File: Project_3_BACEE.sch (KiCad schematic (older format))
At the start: 13 parts, among them U1 24LC1025, U2 24LC1025, U3 DS1337S+, U4 ATMEGA328P-AU, Y1 Crystal 32 MHz, Y2 Crystal 16 MHz

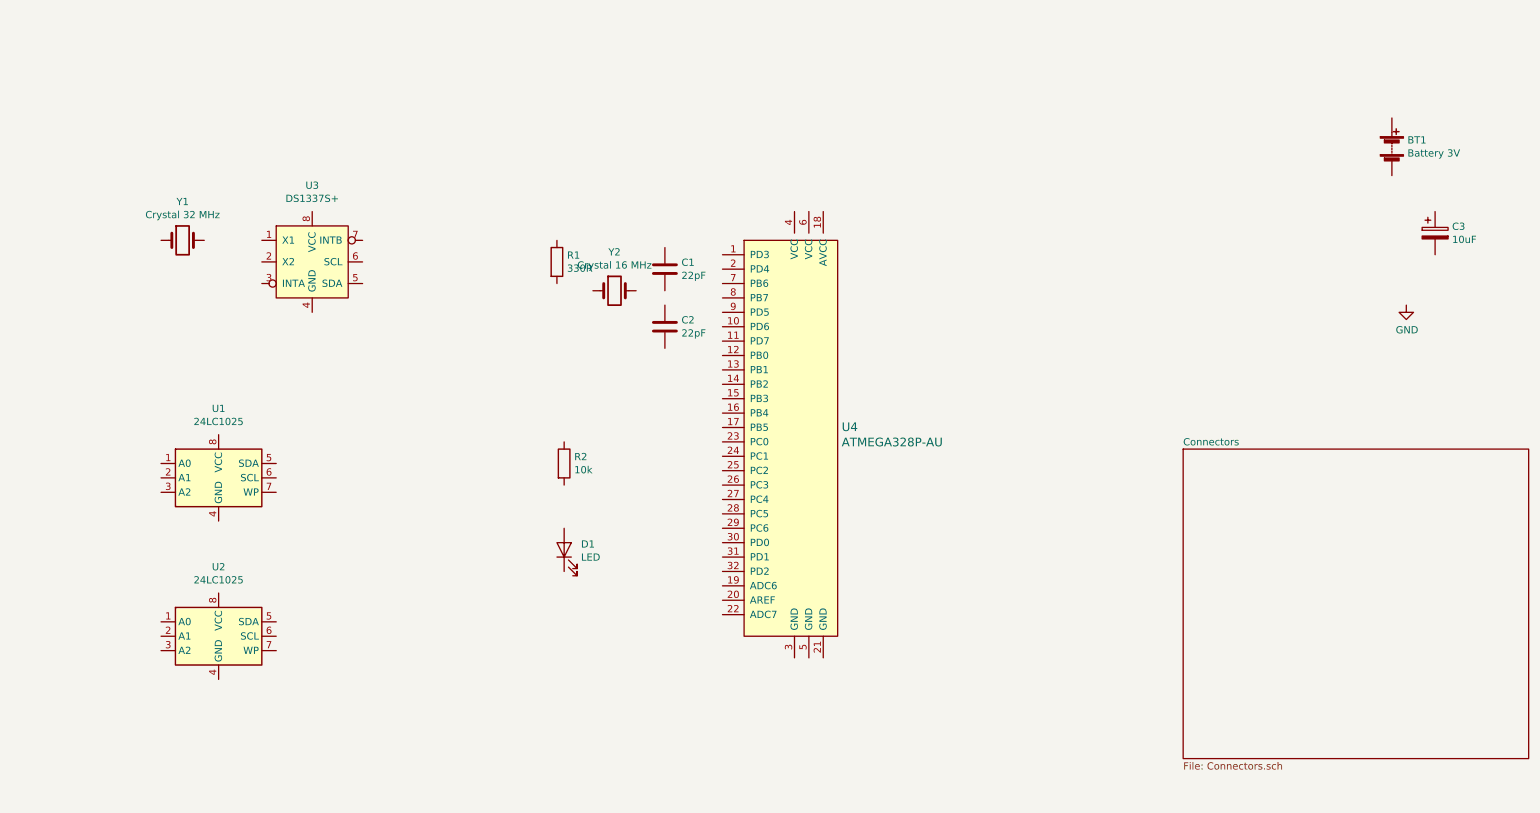
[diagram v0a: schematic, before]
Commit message: Completed wiring and connectors sheet.
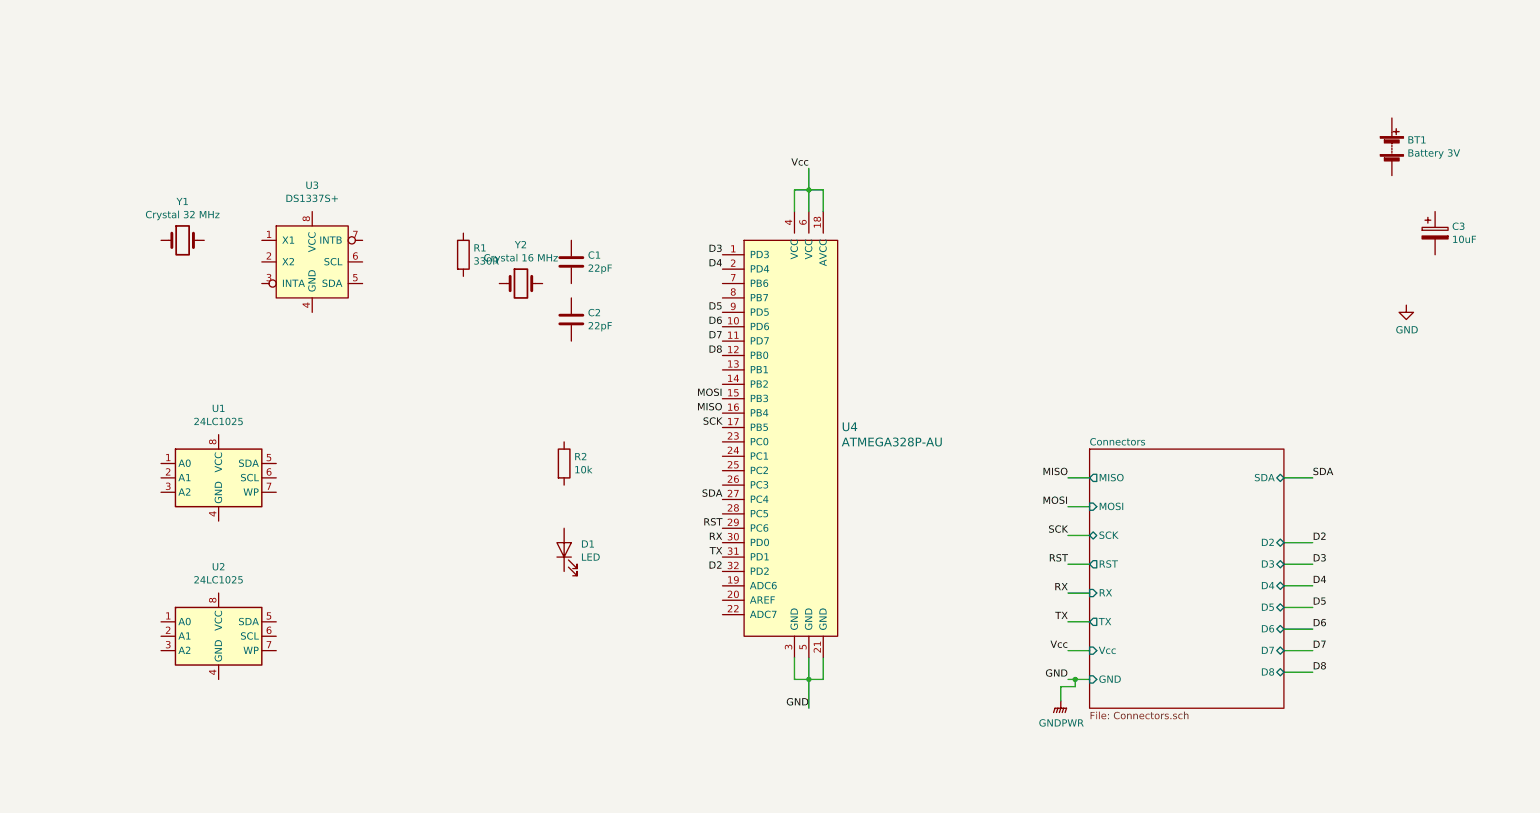
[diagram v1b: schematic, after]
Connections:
- net GND: now also U4.21 (GND), U4.3 (GND), U4.5 (GND)
- net D3: now reaches U4.1 (PD3)
- net D6: now reaches U4.10 (PD6)
- net D7: now reaches U4.11 (PD7)
- net D8: now reaches U4.12 (PB0)
- net MOSI: now reaches U4.15 (PB3)
- net MISO: now reaches U4.16 (PB4)
- net SCK: now reaches U4.17 (PB5)
- net Vcc: now reaches U4.18 (AVCC)
- net Vcc: now also U4.4 (VCC), U4.6 (VCC)
- net D4: now reaches U4.2 (PD4)
- net SDA: now reaches U4.27 (PC4)
- net RST: now reaches U4.29 (PC6)
- net RX: now reaches U4.30 (PD0)
- net TX: now reaches U4.31 (PD1)
- net D2: now reaches U4.32 (PD2)
- net D5: now reaches U4.9 (PD5)
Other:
- moved on the sheet: C1, C2, R1, Y2
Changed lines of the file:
@@
 L Device:C C1
 U 1 1 5D837139
-P 5100 2650
-F 0 "C1" H 5215 2696 50  0000 L CNN
-F 1 "22pF" H 5215 2605 50  0000 L CNN
-F 2 "Capacitor_SMD:C_0805_2012Metric_Pad1.15x1.40mm_HandSolder" H 5138 2500 50  0001 C CNN
-F 3 "~" H 5100 2650 50  0001 C CNN
-	1    5100 2650
+P 4450 2600
+F 0 "C1" H 4565 2646 50  0000 L CNN
+F 1 "22pF" H 4565 2555 50  0000 L CNN
+F 2 "Capacitor_SMD:C_0805_2012Metric_Pad1.15x1.40mm_HandSolder" H 4488 2450 50  0001 C CNN
+F 3 "~" H 4450 2600 50  0001 C CNN
+	1    4450 2600
 	1    0    0    -1
 $EndComp
@@
 L Device:C C2
 U 1 1 5D837758
-P 5100 3050
-F 0 "C2" H 5215 3096 50  0000 L CNN
-F 1 "22pF" H 5215 3005 50  0000 L CNN
-F 2 "Capacitor_SMD:C_0805_2012Metric_Pad1.15x1.40mm_HandSolder" H 5138 2900 50  0001 C CNN
-F 3 "~" H 5100 3050 50  0001 C CNN
-	1    5100 3050
+P 4450 3000
+F 0 "C2" H 4565 3046 50  0000 L CNN
+F 1 "22pF" H 4565 2955 50  0000 L CNN
+F 2 "Capacitor_SMD:C_0805_2012Metric_Pad1.15x1.40mm_HandSolder" H 4488 2850 50  0001 C CNN
+F 3 "~" H 4450 3000 50  0001 C CNN
+	1    4450 3000
 	1    0    0    -1
 $EndComp
@@
 L Device:R R1
 U 1 1 5D8396B9
-P 4350 2600
-F 0 "R1" H 4420 2646 50  0000 L CNN
-F 1 "330R" H 4420 2555 50  0000 L CNN
-F 2 "Resistor_SMD:R_0805_2012Metric_Pad1.15x1.40mm_HandSolder" V 4280 2600 50  0001 C CNN
-F 3 "~" H 4350 2600 50  0001 C CNN
-	1    4350 2600
+P 3700 2550
+F 0 "R1" H 3770 2596 50  0000 L CNN
+F 1 "330R" H 3770 2505 50  0000 L CNN
+F 2 "Resistor_SMD:R_0805_2012Metric_Pad1.15x1.40mm_HandSolder" V 3630 2550 50  0001 C CNN
+F 3 "~" H 3700 2550 50  0001 C CNN
+	1    3700 2550
 	1    0    0    -1
 $EndComp
@@
 	1    0    0    -1
 $EndComp
-$Sheet
-S 8700 3900 2400 2150
-U 5D83B0D5
-F0 "Connectors" 50
-F1 "Connectors.sch" 50
-$EndSheet
 $Comp
 L dk_Embedded-Microcontrollers:ATMEGA328P-AU U4
@@
 L Device:Crystal Y2
 U 1 1 5D83E859
-P 4750 2800
-F 0 "Y2" H 4750 3068 50  0000 C CNN
-F 1 "Crystal 16 MHz" H 4750 2977 50  0000 C CNN
-F 2 "Crystal:Crystal_SMD_5032-2Pin_5.0x3.2mm_HandSoldering" H 4750 2800 50  0001 C CNN
-F 3 "~" H 4750 2800 50  0001 C CNN
-	1    4750 2800
+P 4100 2750
+F 0 "Y2" H 4100 3018 50  0000 C CNN
+F 1 "Crystal 16 MHz" H 4100 2927 50  0000 C CNN
+F 2 "Crystal:Crystal_SMD_5032-2Pin_5.0x3.2mm_HandSoldering" H 4100 2750 50  0001 C CNN
+F 3 "~" H 4100 2750 50  0001 C CNN
+	1    4100 2750
 	1    0    0    -1
 $EndComp
@@
 	1    0    0    -1
 $EndComp
+Text Label 7900 4100 2    50   ~ 0
+MISO
+Text Label 5500 3650 2    50   ~ 0
+MISO
+Wire Wire Line
+	8050 4100 7900 4100
+Text Label 7900 4700 2    50   ~ 0
+RST
+Text Label 7900 4300 2    50   ~ 0
+MOSI
+Text Label 7900 5500 2    50   ~ 0
+GND
+Text Label 7900 4500 2    50   ~ 0
+SCK
+Wire Wire Line
+	7900 4500 8050 4500
+Wire Wire Line
+	7900 4700 8050 4700
+Wire Wire Line
+	7900 4300 8050 4300
+Wire Wire Line
+	7900 5500 7950 5500
+Text Label 7900 5300 2    50   ~ 0
+Vcc
+Wire Wire Line
+	7900 5300 8050 5300
+Text Label 5500 3550 2    50   ~ 0
+MOSI
+Text Label 5500 3750 2    50   ~ 0
+SCK
+Text Label 5500 4450 2    50   ~ 0
+RST
+Text Label 6100 1950 2    50   ~ 0
+Vcc
+Wire Wire Line
+	6000 2250 6000 2100
+Wire Wire Line
+	6200 2100 6200 2250
+Wire Wire Line
+	6000 2100 6100 2100
+Wire Wire Line
+	6100 2250 6100 2100
+Connection ~ 6100 2100
+Wire Wire Line
+	6100 2100 6200 2100
+Wire Wire Line
+	6100 2100 6100 1950
+Wire Wire Line
+	6000 5350 6000 5500
+Wire Wire Line
+	6000 5500 6100 5500
+Wire Wire Line
+	6200 5500 6200 5350
+Wire Wire Line
+	6100 5350 6100 5500
+Connection ~ 6100 5500
+Wire Wire Line
+	6100 5500 6200 5500
+Text Label 6100 5700 2    50   ~ 0
+GND
+Wire Wire Line
+	6100 5500 6100 5700
+$Comp
+L power:GNDPWR #PWR?
+U 1 1 5D85B7E3
+P 7850 5650
+F 0 "#PWR?" H 7850 5450 50  0001 C CNN
+F 1 "GNDPWR" H 7854 5496 50  0000 C CNN
+F 2 "" H 7850 5600 50  0001 C CNN
+F 3 "" H 7850 5600 50  0001 C CNN
+	1    7850 5650
+	1    0    0    -1
+$EndComp
+Wire Wire Line
+	7850 5650 7850 5550
+Wire Wire Line
+	7850 5550 7950 5550
+Wire Wire Line
+	7950 5550 7950 5500
+Connection ~ 7950 5500
+Wire Wire Line
+	7950 5500 8050 5500
+Text Label 9600 4100 0    50   ~ 0
+SDA
+Text Label 9600 4550 0    50   ~ 0
+D2
+Text Label 9600 4700 0    50   ~ 0
+D3
+Text Label 9600 4850 0    50   ~ 0
+D4
+Text Label 9600 5000 0    50   ~ 0
+D5
+Text Label 9600 5150 0    50   ~ 0
+D6
+Text Label 9600 5300 0    50   ~ 0
+D7
+Text Label 9600 5450 0    50   ~ 0
+D8
+Text Label 7900 4900 2    50   ~ 0
+RX
+Text Label 7900 5100 2    50   ~ 0
+TX
+Wire Wire Line
+	7900 4900 8050 4900
+Wire Wire Line
+	7900 5100 8050 5100
+Wire Wire Line
+	9600 4100 9400 4100
+Wire Wire Line
+	9600 4550 9400 4550
+Wire Wire Line
+	9600 4700 9400 4700
+Wire Wire Line
+	9600 4850 9400 4850
+Wire Wire Line
+	9600 5000 9400 5000
+Wire Wire Line
+	9600 5150 9400 5150
+Wire Wire Line
+	9600 5300 9400 5300
+Wire Wire Line
+	9600 5450 9400 5450
+Text Label 5500 2550 2    50   ~ 0
+D3
+Text Label 5500 2650 2    50   ~ 0
+D4
+Text Label 5500 2950 2    50   ~ 0
+D5
+Text Label 5500 3050 2    50   ~ 0
+D6
+Text Label 5500 3150 2    50   ~ 0
+D7
+Text Label 5500 3250 2    50   ~ 0
+D8
+Text Label 5500 4250 2    50   ~ 0
+SDA
+Text Label 5500 4550 2    50   ~ 0
+RX
+Text Label 5500 4650 2    50   ~ 0
+TX
+Text Label 5500 4750 2    50   ~ 0
+D2
+$Sheet
+S 8050 3900 1350 1800
+U 5D83B0D5
+F0 "Connectors" 50
+F1 "Connectors.sch" 50
+F2 "SCK" B L 8050 4500 50
+F3 "RST" O L 8050 4700 50
+F4 "Vcc" I L 8050 5300 50
+F5 "MOSI" I L 8050 4300 50
+F6 "GND" I L 8050 5500 50
+F7 "MISO" O L 8050 4100 50
+F8 "RX" I L 8050 4900 50
+F9 "TX" O L 8050 5100 50
+F10 "SDA" B R 9400 4100 50
+F11 "D2" B R 9400 4550 50
+F12 "D3" B R 9400 4700 50
+F13 "D4" B R 9400 4850 50
+F14 "D5" B R 9400 5000 50
+F15 "D6" B R 9400 5150 50
+F16 "D7" B R 9400 5300 50
+F17 "D8" B R 9400 5450 50
+$EndSheet
 $EndSCHEMATC

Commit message: COmpleted wiring in root sheet.
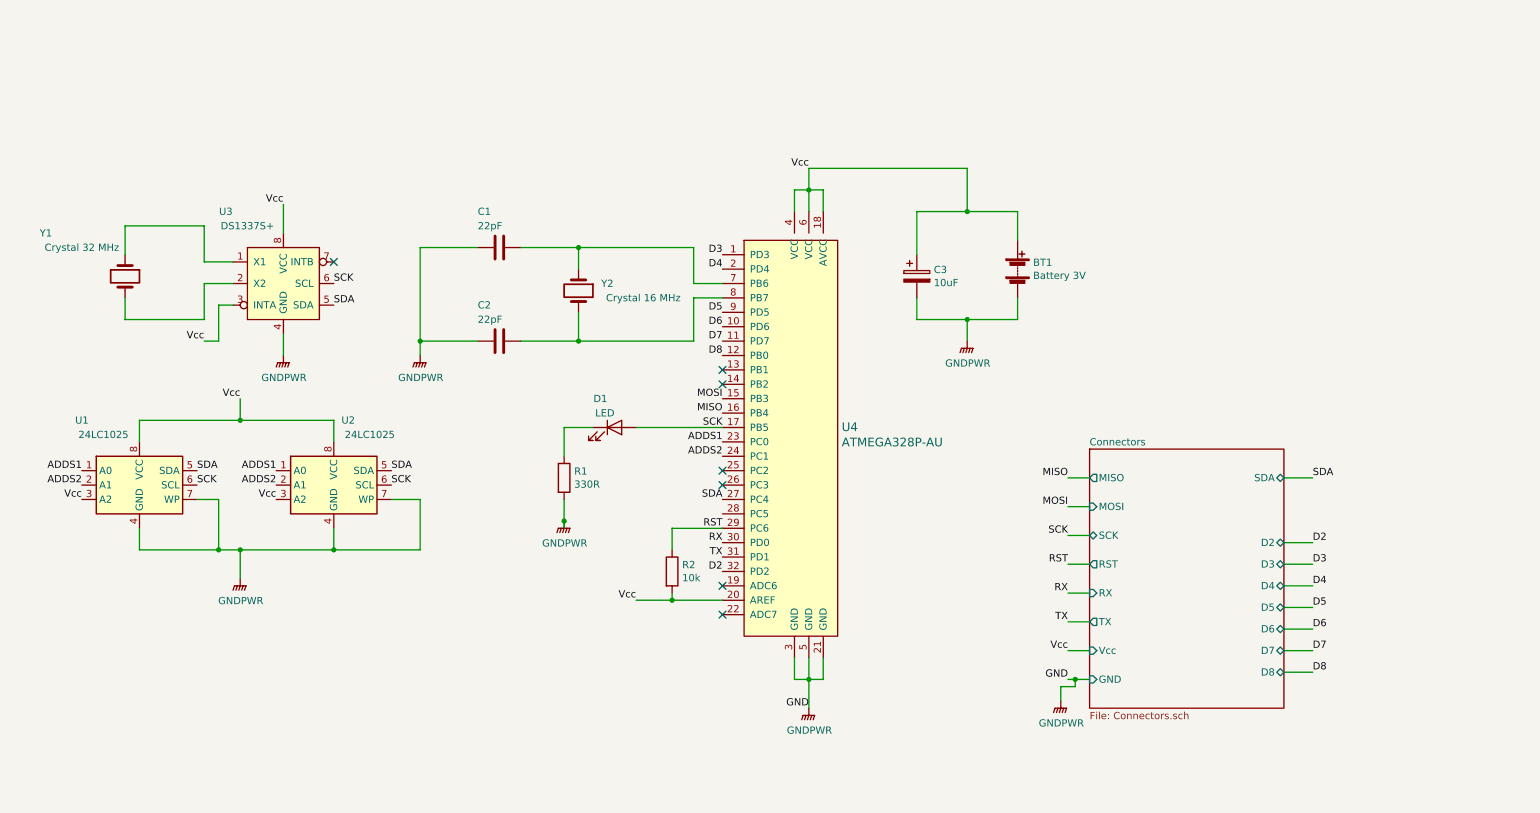
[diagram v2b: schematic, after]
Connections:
- net GND is gone; now on net GNDPWR: U4.21 (GND), U4.3 (GND), U4.5 (GND)
- net RST: now also R2.1
- net SCK: now also D1.2 (A), U1.6 (SCL), U2.6 (SCL), U3.6 (SCL)
- net SDA: now also U1.5 (SDA), U2.5 (SDA), U3.5 (SDA)
- net Vcc: now also BT1.1 (+), C3.1, R2.2, U1.3 (A2), U1.8 (VCC), U2.3 (A2), U2.8 (VCC), U3.3 (INTA), U3.8 (VCC), U4.20 (AREF)
- net GNDPWR: now reaches BT1.2 (-)
- net GNDPWR: now also C1.2, C2.2, C3.2, R1.2, U1.4 (GND), U1.7 (WP), U2.4 (GND), U2.7 (WP), U3.4 (GND)
- net at C1.1: now also U4.7 (PB6), Y2.1
- net at C2.1: now also U4.8 (PB7), Y2.2
- net at D1.1 (K): now also R1.1
- net ADDS1: now reaches U4.23 (PC0)
- net ADDS1: now also U1.1 (A0), U2.1 (A0)
- net ADDS2: now reaches U4.24 (PC1)
- net ADDS2: now also U1.2 (A1), U2.2 (A1)
- net at U3.1 (X1): now also Y1.1
- net at U3.2 (X2): now also Y1.2
- no-connect marks 0 -> 7
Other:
- moved on the sheet: BT1, C1, C2, C3, D1, R1, R2, U1, U2, U3, Y1, Y2

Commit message: Added power flag symbol.
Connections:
- no-connect marks 7 -> 8
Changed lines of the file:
@@
 	6100 5500 6100 5700
 $Comp
-L power:GNDPWR #PWR?
+L power:GNDPWR #PWR0101
 U 1 1 5D85B7E3
 P 7850 5650
-F 0 "#PWR?" H 7850 5450 50  0001 C CNN
+F 0 "#PWR0101" H 7850 5450 50  0001 C CNN
 F 1 "GNDPWR" H 7854 5496 50  0000 C CNN
 F 2 "" H 7850 5600 50  0001 C CNN
@@
 	1350 3000 1350 2850
 $Comp
-L power:GNDPWR #PWR?
+L power:GNDPWR #PWR0102
 U 1 1 5D872EA3
 P 2450 3250
-F 0 "#PWR?" H 2450 3050 50  0001 C CNN
+F 0 "#PWR0102" H 2450 3050 50  0001 C CNN
 F 1 "GNDPWR" H 2454 3096 50  0000 C CNN
 F 2 "" H 2450 3200 50  0001 C CNN
@@
 Connection ~ 2150 3700
 $Comp
-L power:GNDPWR #PWR?
+L power:GNDPWR #PWR0103
 U 1 1 5D88239E
 P 2150 4800
-F 0 "#PWR?" H 2150 4600 50  0001 C CNN
+F 0 "#PWR0103" H 2150 4600 50  0001 C CNN
 F 1 "GNDPWR" H 2154 4646 50  0000 C CNN
 F 2 "" H 2150 4750 50  0001 C CNN
@@
 ADDS2
 $Comp
-L power:GNDPWR #PWR?
+L power:GNDPWR #PWR0104
 U 1 1 5D88C5F3
 P 7200 3150
-F 0 "#PWR?" H 7200 2950 50  0001 C CNN
+F 0 "#PWR0104" H 7200 2950 50  0001 C CNN
 F 1 "GNDPWR" H 7204 2996 50  0000 C CNN
 F 2 "" H 7200 3100 50  0001 C CNN
@@
 	7200 2250 7200 1950
 Wire Wire Line
-	7200 1950 6100 1950
+	7200 1950 6600 1950
 Connection ~ 7200 2250
 Wire Wire Line
@@
 Connection ~ 4500 3150
 $Comp
-L power:GNDPWR #PWR?
+L power:GNDPWR #PWR0105
 U 1 1 5D8B0E36
 P 3400 3250
-F 0 "#PWR?" H 3400 3050 50  0001 C CNN
+F 0 "#PWR0105" H 3400 3050 50  0001 C CNN
 F 1 "GNDPWR" H 3404 3096 50  0000 C CNN
 F 2 "" H 3400 3200 50  0001 C CNN
@@
 	4900 3750 5500 3750
 $Comp
-L power:GNDPWR #PWR?
+L power:GNDPWR #PWR0106
 U 1 1 5D8C41B6
 P 4400 4400
-F 0 "#PWR?" H 4400 4200 50  0001 C CNN
+F 0 "#PWR0106" H 4400 4200 50  0001 C CNN
 F 1 "GNDPWR" H 4404 4246 50  0000 C CNN
 F 2 "" H 4400 4350 50  0001 C CNN
@@
 Connection ~ 5150 4950
 $Comp
-L power:GNDPWR #PWR?
+L power:GNDPWR #PWR0107
 U 1 1 5D8D2EDE
 P 6100 5700
-F 0 "#PWR?" H 6100 5500 50  0001 C CNN
+F 0 "#PWR0107" H 6100 5500 50  0001 C CNN
 F 1 "GNDPWR" H 6104 5546 50  0000 C CNN
 F 2 "" H 6100 5650 50  0001 C CNN
@@
 NoConn ~ 5500 4850
 NoConn ~ 5500 5050
+NoConn ~ 5500 4350
+$Comp
+L power:PWR_FLAG #FLG0101
+U 1 1 5D8E66FC
+P 6600 1800
+F 0 "#FLG0101" H 6600 1875 50  0001 C CNN
+F 1 "PWR_FLAG" H 6600 1973 50  0000 C CNN
+F 2 "" H 6600 1800 50  0001 C CNN
+F 3 "~" H 6600 1800 50  0001 C CNN
+	1    6600 1800
+	1    0    0    -1
+$EndComp
+Wire Wire Line
+	6600 1950 6600 1800
+Connection ~ 6600 1950
+Wire Wire Line
+	6600 1950 6100 1950
 $EndSCHEMATC
